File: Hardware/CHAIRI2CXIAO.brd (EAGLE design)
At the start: 32 x 32 mm, 23 parts, among them IC1 DS3502, IC2 DS3502, J1 OUTPUT, J2 M06-PLAIN

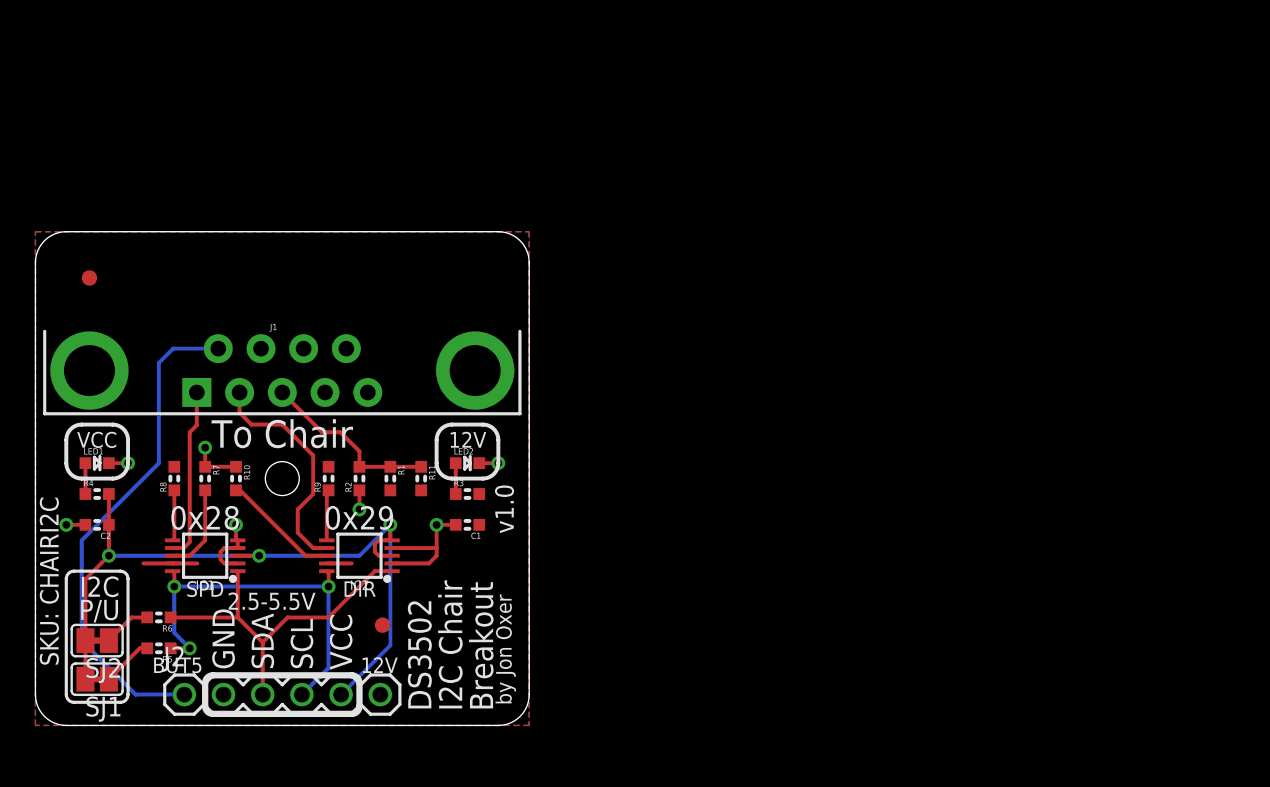
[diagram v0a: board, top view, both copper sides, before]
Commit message: Major conversion to use ESP32 in UB5 plastic box.
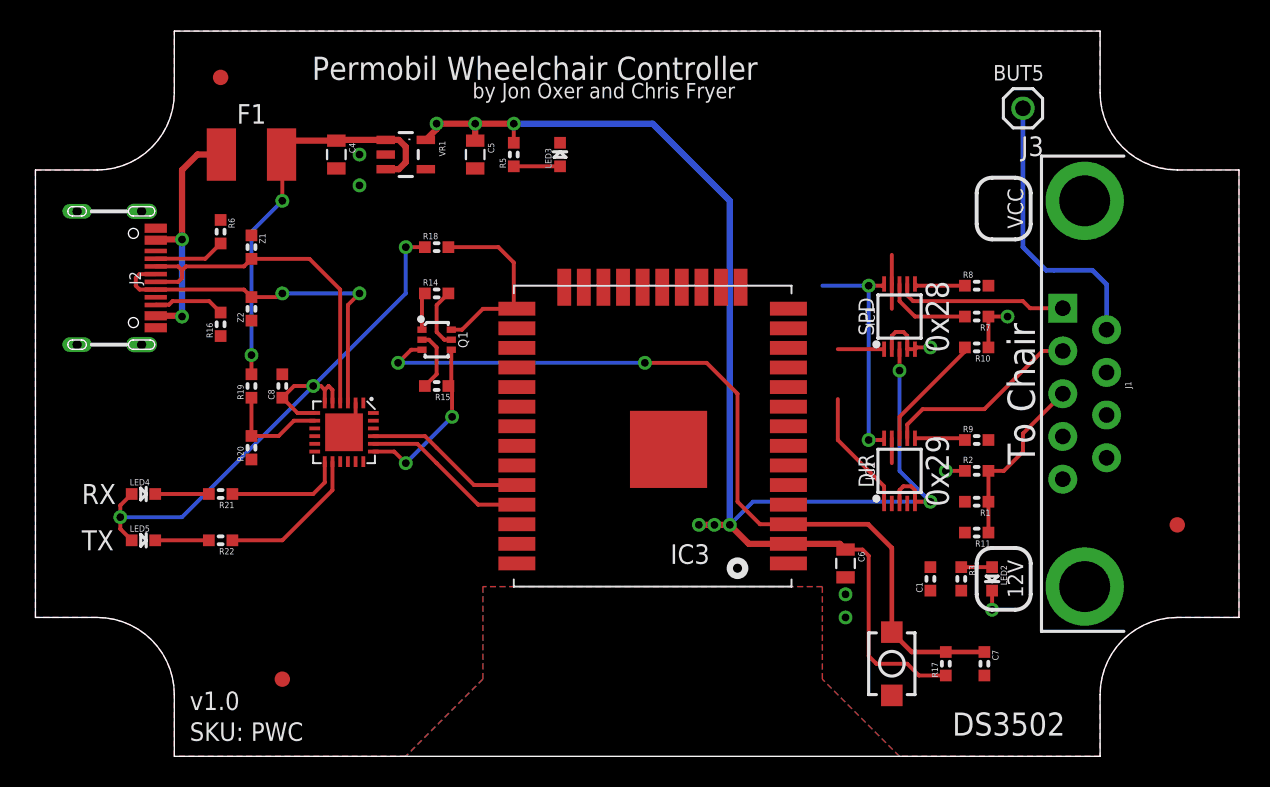
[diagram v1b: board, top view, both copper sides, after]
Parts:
- removed C2: 100nF, SuperHouse-DiscreteSemi:C0603
- removed FID1, FID2: FIDUCIAL1X2.5, SuperHouse-Symbols:FIDUCIAL-1X2.5
- removed LED1: BLUE, SuperHouse-LEDs:LED-0603
- removed R4: 4K7, SuperHouse-DiscreteSemi:R0603
- removed SJ1, SJ2: PU, SuperHouse-Jumpers:SJC
- added C4, C5, C6: 10uF, SuperHouse-DiscreteSemi:C0805
- added C7: 1uF, SuperHouse-DiscreteSemi:C0603
- added C8: 100nF, SuperHouse-DiscreteSemi:C0603
- added F1: 500mA 1812 PTC, SuperHouse-Fuses:1812
- added IC3: ESPWROOM32, SuperHouse-MCUs:ESPWROOM32
- added IC5: CP2102N-A01-GQFN24, SuperHouse-ICs:QFN-24
- added J3: BUT5, SuperHouse-Connectors:1X01
- added LED3: BLUE, SuperHouse-LEDs:LED-0603
- added LED4: RX/GRN, SuperHouse-LEDs:LED-0603
- added LED5: TX/YEL, SuperHouse-LEDs:LED-0603
- added Q1: MMDT3904, SuperHouse-DiscreteSemi:SOT-363
- added R14, R15: 10K, SuperHouse-DiscreteSemi:R0603
- added R16: 5.1K, SuperHouse-DiscreteSemi:R0603
- added R17, R18: 22K, SuperHouse-DiscreteSemi:R0603
- added R19: 22.1K, SuperHouse-DiscreteSemi:R0603
- added R20: 47.5K, SuperHouse-DiscreteSemi:R0603
- added R21, R22: 1K, SuperHouse-DiscreteSemi:R0603
- added S2: RESET, SuperHouse-Switches:TACTILE_SMT_3X4X2
- added U$35, U$36, U$37: FIDUCIAL1X2, SuperHouse-Symbols:FIDUCIAL-1X2
- added VR1: AP2112KSOT25, SuperHouse-Regulators:SOT23-5
- added Z1, Z2: PGB1010603, SuperHouse-DiscreteSemi:TVS0603
- J2: value M06-PLAIN -> USB-C-16P-16P; device SuperHouse-Connectors:1X06 -> SuperHouse-Connectors:USB-C-16P
- R5: value 4K7 -> 10K
- R6: value 4K7 -> 5.1K
- moved R8 53.5 mm to (61.0, 30.5), turned to 0 degrees
- moved J1 52.0 mm to (68.0, 23.5), turned to 270 degrees
- moved R7 51.1 mm to (61.0, 28.5), turned to 180 degrees
- moved R10 48.7 mm to (61.0, 26.5), turned to 180 degrees
- moved IC1 47.6 mm to (56.0, 28.5), turned to 90 degrees
- moved R9 42.1 mm to (61.0, 20.5), turned to 0 degrees
- moved R2 40.0 mm to (61.0, 18.5), turned to 0 degrees
- moved R5 39.4 mm to (31.0, 39.0), turned to 90 degrees
- moved R1 38.0 mm to (61.0, 16.5), turned to 180 degrees
- moved R11 36.2 mm to (61.0, 14.5), turned to 180 degrees
- moved IC2 35.4 mm to (56.0, 18.5), turned to 90 degrees
- moved LED2 34.8 mm to (62.0, 11.5), turned to 270 degrees
- moved R3 32.5 mm to (60.0, 11.5), turned to 270 degrees
- moved C1 30.2 mm to (58.0, 11.5), turned to 90 degrees
- moved J2 30.1 mm to (2.70, 31.0), turned to 270 degrees
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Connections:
- removed net N$5: LED1.A, R4.1
- removed net VCC: C2.1, IC1.3, IC2.3, IC2.5, J2.5, R4.2, SJ1.2, SJ2.2
- new net !RESET: C7.1, IC3.3, Q1.3, R17.2, S2.2
- new net 3.3V: C5.1, C6.1, C8.1, IC1.3, IC2.3, IC2.5, IC3.2, IC5.5, IC5.6, IC5.7, LED4.A, LED5.A, R17.1, R18.1, R5.2, VR1.5
- new net 5V: C4.1, F1.2, R19.2, VR1.1, VR1.3
- new net D+: IC5.3, J2.A6, J2.B6, Z2.2
- new net D-: IC5.4, J2.A7, J2.B7, Z1.2
- new net DTR: IC5.23, Q1.1, R14.1
- new net GPIO0: IC3.25, Q1.6, R18.2
- new net N$10: J2.B5, R16.2
- new net N$11: J2.A5, R6.2
- new net N$13: LED5.C, R22.2
- new net N$39: IC5.8, R19.1, R20.2
- new net N$7: Q1.5, R14.2
- new net N$9: LED4.C, R21.2
- new net RTS: IC5.19, Q1.4, R15.1
- new net RXD0: IC3.34, IC5.21
- new net RX_LED: IC5.13, R21.1
- new net TXD0: IC3.35, IC5.20
- new net TX_LED: IC5.14, R22.1
- new net VIN: F1.1, J2.A4B9, J2.A9B4
- net 12V: no longer J2.6
- net BUT5: now also J3.1; no longer J2.1
- net GND: now also C4.2, C5.2, C6.2, C7.2, C8.2, IC3.1, IC3.15, IC3.38, IC3.GND@4, IC5.2, IC5.TGND, J2.A12B1, J2.A1B12, J2.FIX1, J2.FIX2, J2.FIX3, J2.FIX4, LED3.C, R16.1, R20.1, R6.1, S2.1, VR1.2, Z1.1, Z2.1; no longer C2.2, J2.2, LED1.C
- net N$1: now also LED3.A, R5.1; no longer R5.2, SJ1.1
- net N$8: now also Q1.2, R15.2; no longer R6.2, SJ2.1
- net SCL: now also IC3.36; no longer J2.4, R5.1
- net SDA: now also IC3.33; no longer J2.3, R6.1
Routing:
- net 3.3V: track 0.00 -> 138.2 mm, vias 0 -> 11
- net !RESET: track 0.00 -> 55.0 mm, vias 0 -> 2
- net VCC: track 49.3 -> 0.00 mm, vias 3 -> 0
- net 5V: track 0.00 -> 26.8 mm, vias 0 -> 2
- net D+: track 0.00 -> 24.2 mm, vias 0 -> 2
- net D-: track 0.00 -> 22.8 mm
- net VIN: track 0.00 -> 15.9 mm, vias 0 -> 2
- net BUT5: track 32.4 -> 18.4 mm
- net GPIO0: track 0.00 -> 12.5 mm
- net SDA: track 23.3 -> 11.0 mm
- net RTS: track 0.00 -> 11.2 mm, vias 0 -> 2
- net TXD0: track 0.00 -> 10.9 mm
- net RXD0: track 0.00 -> 10.6 mm
- net SCL: track 25.5 -> 15.1 mm, vias 3 -> 2
- net TX_LED: track 0.00 -> 9.68 mm
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- added copper zone on layer 1, net GND
- removed copper zone on layer 1, net 12V
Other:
- board size 32 x 32 mm -> 78 x 47 mm
- board text added: "(C)2021 SuperHouse Automation"
- board text added: "Permobil Wheelchair Controller"
- board text added: "RX"
- board text added: "SKU: PWC"
- board text added: "TX"
- board text added: "by Jon Oxer and Chris Fryer"
- board text added: "www.superhouse.tv/pwc"
- board text removed: "(C)2020 SuperHouse Automation"
- board text removed: "2.5-5.5V"
- board text removed: "Breakout"
- board text removed: "GND"
- board text removed: "I2C"
- board text removed: "I2C Chair"
- board text removed: "P/U"
- board text removed: "SCL"
- board text removed: "SDA"
- board text removed: "SKU: CHAIRI2C"
- board text removed: "by Jon Oxer"
- board text removed: "www.superhouse.tv/chairi2c"
